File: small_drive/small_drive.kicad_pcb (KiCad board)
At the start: 2 copper layers, 100 x 80 mm, 175 parts, among them J1 DB9, J2 DB15, M1 SiR826DP, M2 SiR826DP, M3 SiR826DP, M4 SiR826DP, M5 SiR826DP, M6 SiR826DP, P1 CONN_01X04, P2 CONN_01X04, P3 CONN_01X04, P4 CONN_01X04, P5 CONN_01X02, P6 CONN_01X02, P7 CONN_01X02, P8 CONN_01X01, U1 XMC4400-F100, U10 LM5106, U11 ACS711KLCTR-12AB-T, U12 ACS711ELCTR-12AB-T, U13 ACS711KLCTR-12AB-T, U14 AD8226, U15 MAX3463, U16 AMC1203, U17 7805, U18 LT1764EQ, U19 KSZ8081, U2 ips511g, U20 ETH100_MAG, U21 MAX3463, U22 MAX3463, U23 MAX3463, U3 ips511g, U4 MAX3463, U5 AD8226, U6 LT1764EQ, U7 MC33074DTBR2, U8 LM5106, U9 LM5106, X1 NKE1212DC, X2 NKE1212DC, X3 HCPL0201, X4 HCPL0201, X5 HCPL0201, X6 HCPL0201, Y1 12MHz, Y2 25MHz

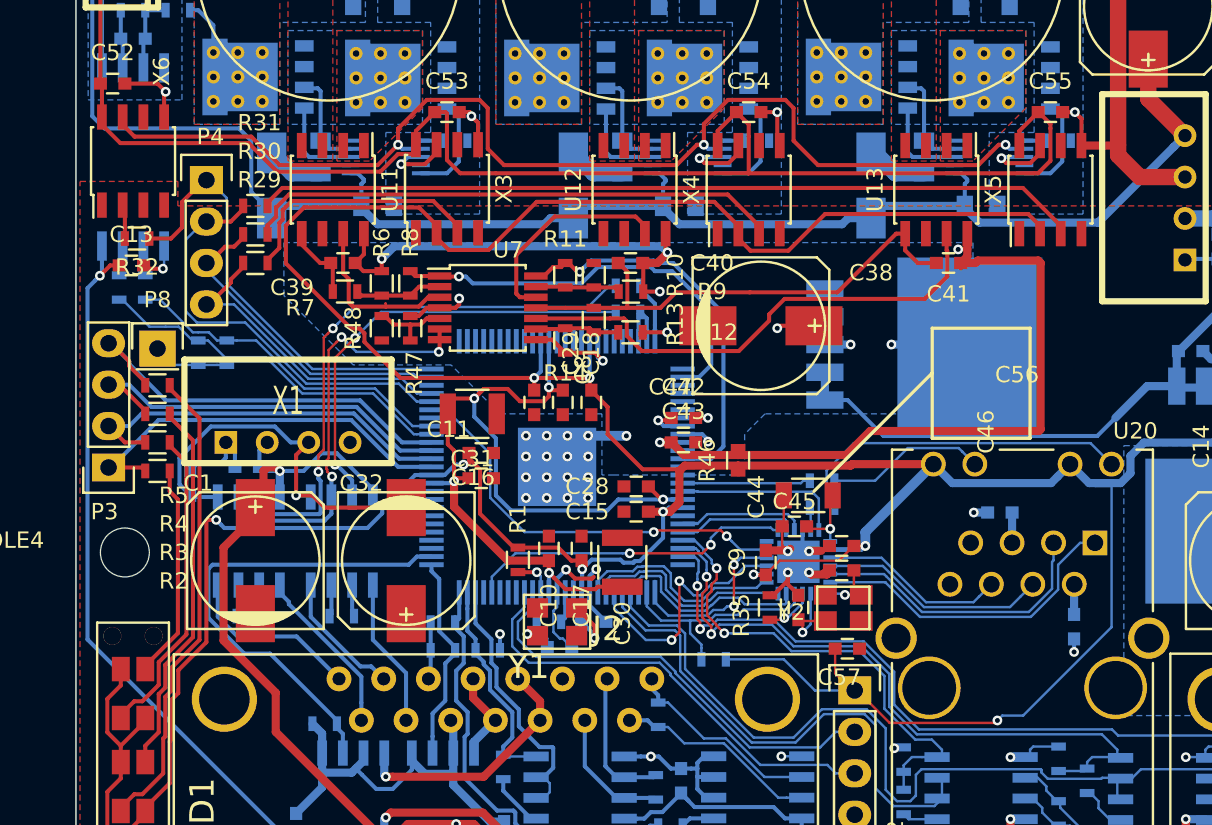
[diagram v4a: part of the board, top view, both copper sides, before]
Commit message: Use 5V for opamp supply.
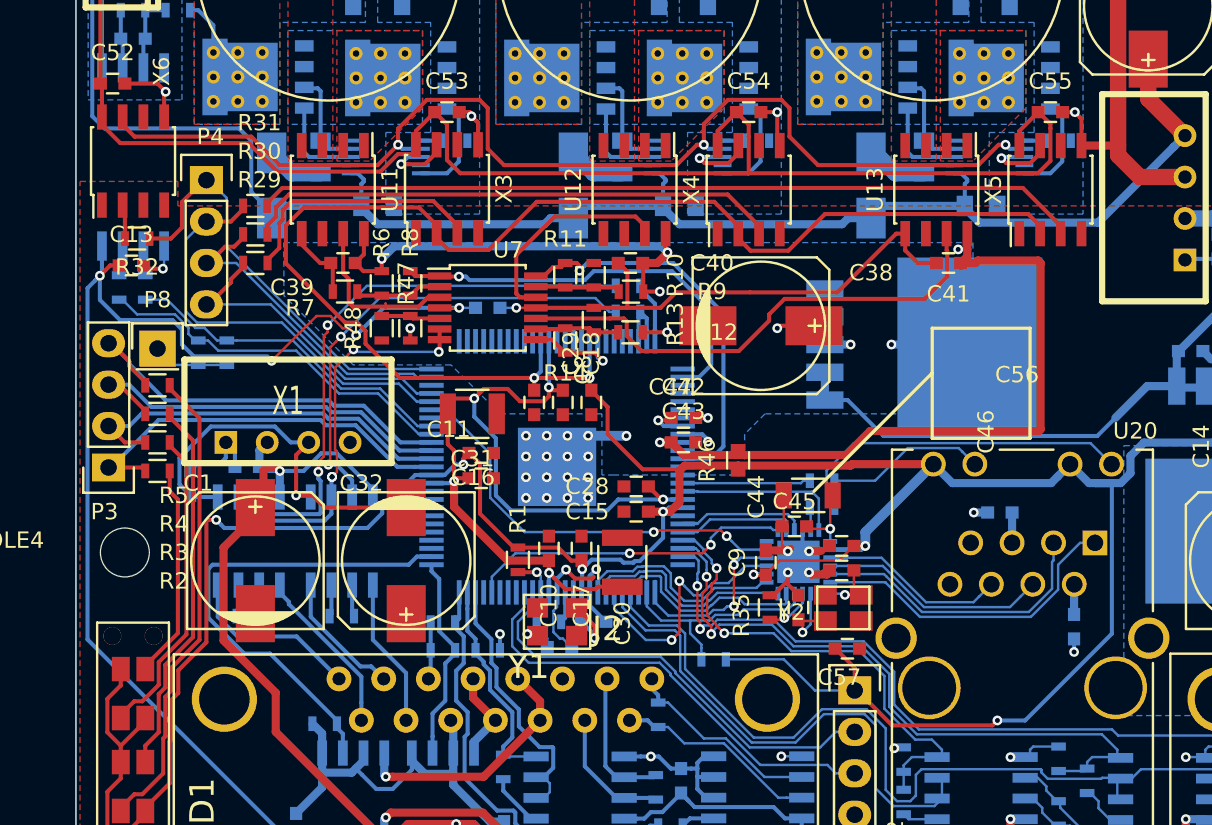
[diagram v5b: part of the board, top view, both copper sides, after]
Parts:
- added C62: 100nF, Capacitors_SMD:C_0603, B.Cu at (64.2, 150.0)
- turned R47 to 90 degrees
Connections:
- U7 pad 4: +3.3VADC -> +5V
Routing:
- net +5V: track 222.4 -> 252.6 mm, vias 7 -> 10
- net +3.3VADC: track 85.2 -> 82.3 mm
- net GND: track 173.1 -> 175.3 mm, vias 38 -> 39
- net Net-(R47-Pad2): track 5.55 -> 3.61 mm
- net Net-(R45-Pad2): track 27.4 -> 29.2 mm
- net Net-(U14-Pad6): track 27.8 -> 26.2 mm, vias 3 -> 4
- net /HBEN: track 27.7 -> 26.4 mm
